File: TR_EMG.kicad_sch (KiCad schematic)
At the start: 7 parts, among them J1 1727230, J2 1727230, J3 1844236, J4 MJ-3523-SMT-TR, J5 MJ-3523-SMT-TR, J6 MJ-3523-SMT-TR, J7 MJ-3523-SMT-TR

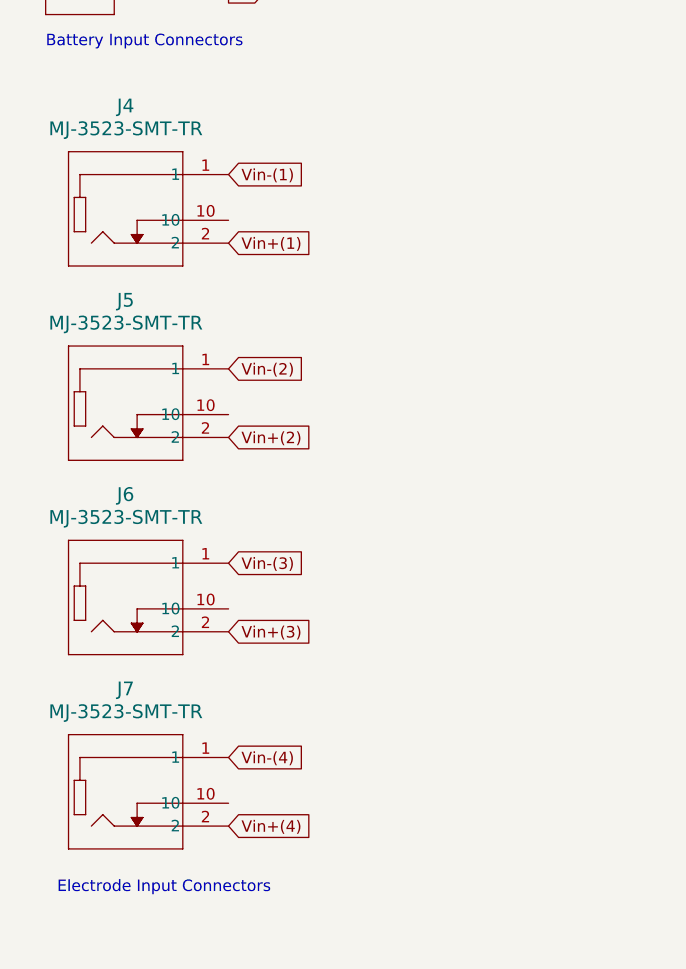
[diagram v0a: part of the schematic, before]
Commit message: first chunk of pcb layout and schematics mods (no connects on pins and changing global labels to hieracarchical labels), one filtering pcb circuit layed out
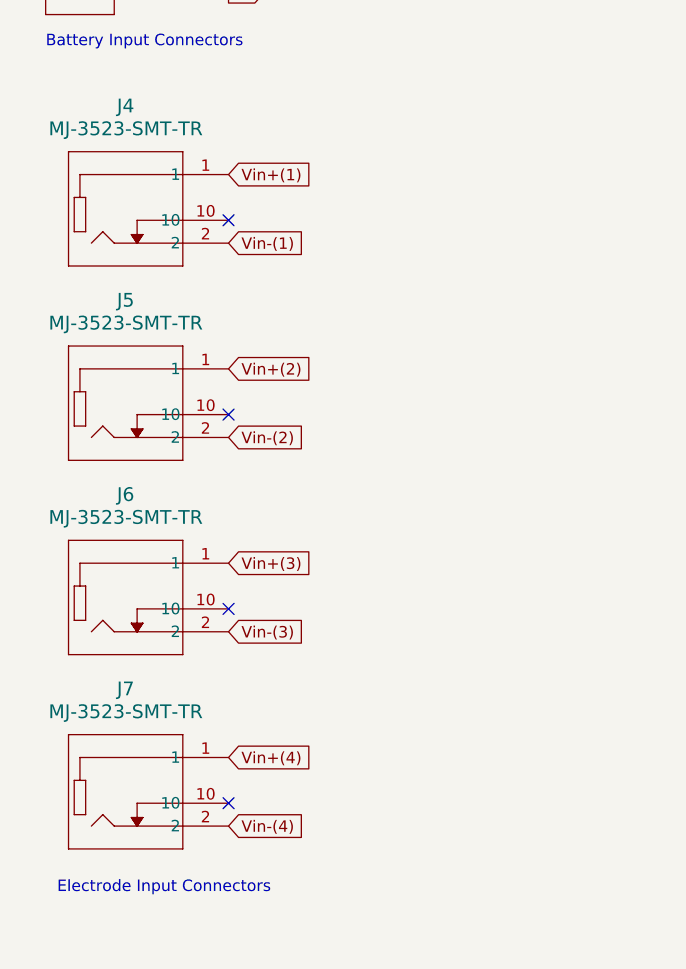
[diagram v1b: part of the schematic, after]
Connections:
- net Vin+(1): now also J4.1; no longer J4.2
- net Vin+(2): now also J5.1; no longer J5.2
- net Vin+(3): now also J6.1; no longer J6.2
- net Vin+(4): now also J7.1; no longer J7.2
- net Vin-(1): now also J4.2; no longer J4.1
- net Vin-(2): now also J5.2; no longer J5.1
- net Vin-(3): now also J6.2; no longer J6.1
- net Vin-(4): now also J7.2; no longer J7.1
- no-connect marks 0 -> 4
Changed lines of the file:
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@@
   (junction (at 30.48 34.29) (diameter 0) (color 0 0 0 0)
   )
+  (no_connect (at 38.1 68.58))
+  (no_connect (at 38.1 133.35))
+  (no_connect (at 38.1 90.17))
+  (no_connect (at 38.1 111.76))
   (wire (pts (xy 262.89 66.04) (xy 269.24 66.04))
     (stroke (width 0) (type default))
@@
     )
   )
+  (global_label "Vin+(3)" (shape input) (at 38.1 106.68 0) (fields_autoplaced)
+    (effects (font (size 1.27 1.27)) (justify left))
+    (property "Intersheetrefs" "${INTERSHEET_REFS}" (at 48.4029 106.68 0)
+      (effects (font (size 1.27 1.27)) (justify left) hide)
+    )
+  )
   (global_label "Vin+(2)" (shape input) (at 157.48 73.66 180) (fields_autoplaced)
     (effects (font (size 1.27 1.27)) (justify right))
@@
     )
   )
-  (global_label "Vin-(1)" (shape input) (at 38.1 63.5 0) (fields_autoplaced)
+  (global_label "Vin-(3)" (shape input) (at 38.1 114.3 0) (fields_autoplaced)
+    (effects (font (size 1.27 1.27)) (justify left))
+    (property "Intersheetrefs" "${INTERSHEET_REFS}" (at 48.4029 114.3 0)
+      (effects (font (size 1.27 1.27)) (justify left) hide)
+    )
+  )
+  (global_label "V-" (shape output) (at 38.1 43.18 0) (fields_autoplaced)
+    (effects (font (size 1.27 1.27)) (justify left))
+    (property "Intersheetrefs" "${INTERSHEET_REFS}" (at 43.7462 43.18 0)
+      (effects (font (size 1.27 1.27)) (justify left) hide)
+    )
+  )
+  (global_label "V-" (shape input) (at 187.96 80.01 270) (fields_autoplaced)
+    (effects (font (size 1.27 1.27)) (justify right))
+    (property "Intersheetrefs" "${INTERSHEET_REFS}" (at 187.96 85.6562 90)
+      (effects (font (size 1.27 1.27)) (justify right) hide)
+    )
+  )
+  (global_label "Vin-(1)" (shape input) (at 38.1 71.12 0) (fields_autoplaced)
+    (effects (font (size 1.27 1.27)) (justify left))
+    (property "Intersheetrefs" "${INTERSHEET_REFS}" (at 48.4029 71.12 0)
+      (effects (font (size 1.27 1.27)) (justify left) hide)
+    )
+  )
+  (global_label "Vin+(1)" (shape input) (at 157.48 41.91 180) (fields_autoplaced)
+    (effects (font (size 1.27 1.27)) (justify right))
+    (property "Intersheetrefs" "${INTERSHEET_REFS}" (at 147.1771 41.91 0)
+      (effects (font (size 1.27 1.27)) (justify right) hide)
+    )
+  )
+  (global_label "Vin+(4)" (shape input) (at 157.48 137.16 180) (fields_autoplaced)
+    (effects (font (size 1.27 1.27)) (justify right))
+    (property "Intersheetrefs" "${INTERSHEET_REFS}" (at 147.1771 137.16 0)
+      (effects (font (size 1.27 1.27)) (justify right) hide)
+    )
+  )
+  (global_label "Vin-(2)" (shape input) (at 157.48 67.31 180) (fields_autoplaced)
+    (effects (font (size 1.27 1.27)) (justify right))
+    (property "Intersheetrefs" "${INTERSHEET_REFS}" (at 147.1771 67.31 0)
+      (effects (font (size 1.27 1.27)) (justify right) hide)
+    )
+  )
+  (global_label "Vin+(2)" (shape input) (at 38.1 85.09 0) (fields_autoplaced)
+    (effects (font (size 1.27 1.27)) (justify left))
+    (property "Intersheetrefs" "${INTERSHEET_REFS}" (at 48.4029 85.09 0)
+      (effects (font (size 1.27 1.27)) (justify left) hide)
+    )
+  )
+  (global_label "V+" (shape output) (at 33.02 24.13 0) (fields_autoplaced)
+    (effects (font (size 1.27 1.27)) (justify left))
+    (property "Intersheetrefs" "${INTERSHEET_REFS}" (at 38.6662 24.13 0)
+      (effects (font (size 1.27 1.27)) (justify left) hide)
+    )
+  )
+  (global_label "V+" (shape input) (at 187.96 29.21 90) (fields_autoplaced)
+    (effects (font (size 1.27 1.27)) (justify left))
+    (property "Intersheetrefs" "${INTERSHEET_REFS}" (at 187.96 23.5638 90)
+      (effects (font (size 1.27 1.27)) (justify left) hide)
+    )
+  )
+  (global_label "Vin+(4)" (shape input) (at 38.1 128.27 0) (fields_autoplaced)
+    (effects (font (size 1.27 1.27)) (justify left))
+    (property "Intersheetrefs" "${INTERSHEET_REFS}" (at 48.4029 128.27 0)
+      (effects (font (size 1.27 1.27)) (justify left) hide)
+    )
+  )
+  (global_label "Vin+(1)" (shape input) (at 38.1 63.5 0) (fields_autoplaced)
     (effects (font (size 1.27 1.27)) (justify left))
     (property "Intersheetrefs" "${INTERSHEET_REFS}" (at 48.4029 63.5 0)
@@
     )
   )
-  (global_label "Vin+(3)" (shape input) (at 38.1 114.3 0) (fields_autoplaced)
-    (effects (font (size 1.27 1.27)) (justify left))
-    (property "Intersheetrefs" "${INTERSHEET_REFS}" (at 48.4029 114.3 0)
-      (effects (font (size 1.27 1.27)) (justify left) hide)
-    )
-  )
-  (global_label "V-" (shape output) (at 38.1 43.18 0) (fields_autoplaced)
-    (effects (font (size 1.27 1.27)) (justify left))
-    (property "Intersheetrefs" "${INTERSHEET_REFS}" (at 43.7462 43.18 0)
-      (effects (font (size 1.27 1.27)) (justify left) hide)
-    )
-  )
-  (global_label "Vin-(2)" (shape input) (at 38.1 85.09 0) (fields_autoplaced)
-    (effects (font (size 1.27 1.27)) (justify left))
-    (property "Intersheetrefs" "${INTERSHEET_REFS}" (at 48.4029 85.09 0)
-      (effects (font (size 1.27 1.27)) (justify left) hide)
-    )
-  )
-  (global_label "V-" (shape input) (at 187.96 80.01 270) (fields_autoplaced)
-    (effects (font (size 1.27 1.27)) (justify right))
-    (property "Intersheetrefs" "${INTERSHEET_REFS}" (at 187.96 85.6562 90)
-      (effects (font (size 1.27 1.27)) (justify right) hide)
-    )
-  )
-  (global_label "Vin-(3)" (shape input) (at 38.1 106.68 0) (fields_autoplaced)
-    (effects (font (size 1.27 1.27)) (justify left))
-    (property "Intersheetrefs" "${INTERSHEET_REFS}" (at 48.4029 106.68 0)
-      (effects (font (size 1.27 1.27)) (justify left) hide)
-    )
-  )
-  (global_label "Vin+(1)" (shape input) (at 157.48 41.91 180) (fields_autoplaced)
-    (effects (font (size 1.27 1.27)) (justify right))
-    (property "Intersheetrefs" "${INTERSHEET_REFS}" (at 147.1771 41.91 0)
-      (effects (font (size 1.27 1.27)) (justify right) hide)
-    )
-  )
-  (global_label "Vin+(4)" (shape input) (at 157.48 137.16 180) (fields_autoplaced)
-    (effects (font (size 1.27 1.27)) (justify right))
-    (property "Intersheetrefs" "${INTERSHEET_REFS}" (at 147.1771 137.16 0)
-      (effects (font (size 1.27 1.27)) (justify right) hide)
-    )
-  )
-  (global_label "Vin-(2)" (shape input) (at 157.48 67.31 180) (fields_autoplaced)
-    (effects (font (size 1.27 1.27)) (justify right))
-    (property "Intersheetrefs" "${INTERSHEET_REFS}" (at 147.1771 67.31 0)
-      (effects (font (size 1.27 1.27)) (justify right) hide)
-    )
-  )
-  (global_label "V+" (shape output) (at 33.02 24.13 0) (fields_autoplaced)
-    (effects (font (size 1.27 1.27)) (justify left))
-    (property "Intersheetrefs" "${INTERSHEET_REFS}" (at 38.6662 24.13 0)
-      (effects (font (size 1.27 1.27)) (justify left) hide)
-    )
-  )
-  (global_label "V+" (shape input) (at 187.96 29.21 90) (fields_autoplaced)
-    (effects (font (size 1.27 1.27)) (justify left))
-    (property "Intersheetrefs" "${INTERSHEET_REFS}" (at 187.96 23.5638 90)
-      (effects (font (size 1.27 1.27)) (justify left) hide)
-    )
-  )
   (global_label "V+" (shape input) (at 187.96 124.46 90) (fields_autoplaced)
     (effects (font (size 1.27 1.27)) (justify left))
@@
     )
   )
-  (global_label "Vin+(4)" (shape input) (at 38.1 135.89 0) (fields_autoplaced)
+  (global_label "V-" (shape input) (at 187.96 143.51 270) (fields_autoplaced)
+    (effects (font (size 1.27 1.27)) (justify right))
+    (property "Intersheetrefs" "${INTERSHEET_REFS}" (at 187.96 149.1562 90)
+      (effects (font (size 1.27 1.27)) (justify right) hide)
+    )
+  )
+  (global_label "Vin-(4)" (shape input) (at 38.1 135.89 0) (fields_autoplaced)
     (effects (font (size 1.27 1.27)) (justify left))
     (property "Intersheetrefs" "${INTERSHEET_REFS}" (at 48.4029 135.89 0)
@@
     )
   )
-  (global_label "V-" (shape input) (at 187.96 143.51 270) (fields_autoplaced)
-    (effects (font (size 1.27 1.27)) (justify right))
-    (property "Intersheetrefs" "${INTERSHEET_REFS}" (at 187.96 149.1562 90)
-      (effects (font (size 1.27 1.27)) (justify right) hide)
-    )
-  )
-  (global_label "Vin-(4)" (shape input) (at 38.1 128.27 0) (fields_autoplaced)
-    (effects (font (size 1.27 1.27)) (justify left))
-    (property "Intersheetrefs" "${INTERSHEET_REFS}" (at 48.4029 128.27 0)
-      (effects (font (size 1.27 1.27)) (justify left) hide)
-    )
-  )
-  (global_label "Vin+(1)" (shape input) (at 38.1 71.12 0) (fields_autoplaced)
-    (effects (font (size 1.27 1.27)) (justify left))
-    (property "Intersheetrefs" "${INTERSHEET_REFS}" (at 48.4029 71.12 0)
+  (global_label "Vin-(2)" (shape input) (at 38.1 92.71 0) (fields_autoplaced)
+    (effects (font (size 1.27 1.27)) (justify left))
+    (property "Intersheetrefs" "${INTERSHEET_REFS}" (at 48.4029 92.71 0)
       (effects (font (size 1.27 1.27)) (justify left) hide)
     )
@@
       (effects (font (size 1.27 1.27)) (justify left) hide)
     )
-  )
-  (global_label "Vin+(2)" (shape input) (at 38.1 92.71 0) (fields_autoplaced)
-    (effects (font (size 1.27 1.27)) (justify left))
-    (property "Intersheetrefs" "${INTERSHEET_REFS}" (at 48.4029 92.71 0)
-      (effects (font (size 1.27 1.27)) (justify left) hide)
-    )

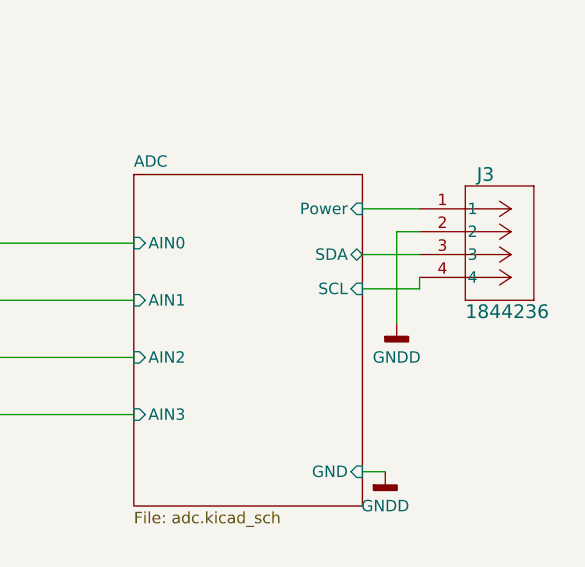
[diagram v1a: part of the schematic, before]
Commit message: finished majority of layout, pcb expanded to four copper layers to accomadate power planes
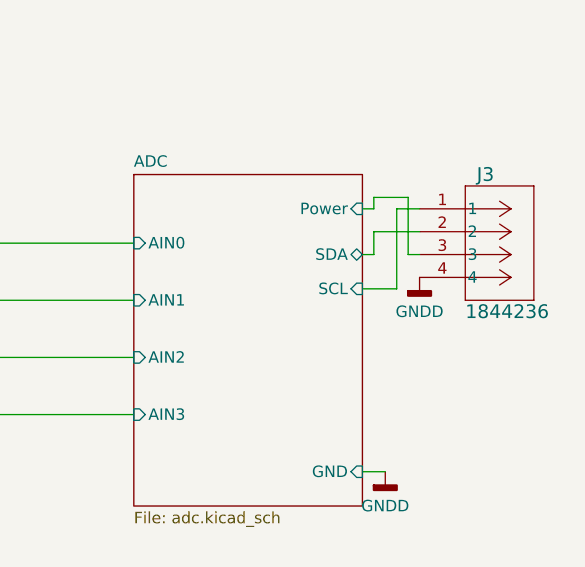
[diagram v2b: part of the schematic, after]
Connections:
- net ADC/Power: now also J3.3; no longer J3.1
- net ADC/SCL: now also J3.1; no longer J3.4
- net ADC/SDA: now also J3.2; no longer J3.3
- net GNDD: now also J3.4; no longer J3.2
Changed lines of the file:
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@@
   (no_connect (at 38.1 90.17))
   (no_connect (at 38.1 111.76))
-  (wire (pts (xy 262.89 66.04) (xy 269.24 66.04))
+  (wire (pts (xy 267.97 66.04) (xy 269.24 66.04))
     (stroke (width 0) (type default))
   )
@@
     (stroke (width 0) (type default))
   )
-  (wire (pts (xy 262.89 69.85) (xy 269.24 69.85))
+  (wire (pts (xy 262.89 60.96) (xy 264.16 60.96))
     (stroke (width 0) (type default))
   )
@@
     (stroke (width 0) (type default))
   )
+  (wire (pts (xy 264.16 59.69) (xy 267.97 59.69))
+    (stroke (width 0) (type default))
+  )
+  (wire (pts (xy 266.7 69.85) (xy 266.7 60.96))
+    (stroke (width 0) (type default))
+  )
   (wire (pts (xy 30.48 34.29) (xy 30.48 40.64))
     (stroke (width 0) (type default))
   )
+  (wire (pts (xy 264.16 66.04) (xy 264.16 63.5))
+    (stroke (width 0) (type default))
+  )
   (wire (pts (xy 187.96 124.46) (xy 187.96 125.73))
     (stroke (width 0) (type default))
@@
     (stroke (width 0) (type default))
   )
-  (wire (pts (xy 269.24 63.5) (xy 266.7 63.5))
-    (stroke (width 0) (type default))
-  )
   (wire (pts (xy 193.04 134.62) (xy 220.98 134.62))
     (stroke (width 0) (type default))
@@
     (stroke (width 0) (type default))
   )
-  (wire (pts (xy 269.24 68.58) (xy 269.24 69.85))
-    (stroke (width 0) (type default))
-  )
   (wire (pts (xy 237.49 64.77) (xy 207.01 64.77))
     (stroke (width 0) (type default))
   )
+  (wire (pts (xy 264.16 60.96) (xy 264.16 59.69))
+    (stroke (width 0) (type default))
+  )
+  (wire (pts (xy 267.97 59.69) (xy 267.97 66.04))
+    (stroke (width 0) (type default))
+  )
   (wire (pts (xy 207.01 102.87) (xy 207.01 77.47))
     (stroke (width 0) (type default))
@@
     (stroke (width 0) (type default))
   )
+  (wire (pts (xy 262.89 66.04) (xy 264.16 66.04))
+    (stroke (width 0) (type default))
+  )
   (wire (pts (xy 187.96 110.49) (xy 187.96 111.76))
     (stroke (width 0) (type default))
   )
-  (wire (pts (xy 266.7 63.5) (xy 266.7 73.66))
-    (stroke (width 0) (type default))
-  )
-  (wire (pts (xy 262.89 60.96) (xy 269.24 60.96))
+  (wire (pts (xy 262.89 69.85) (xy 266.7 69.85))
+    (stroke (width 0) (type default))
+  )
+  (wire (pts (xy 266.7 60.96) (xy 269.24 60.96))
     (stroke (width 0) (type default))
   )
@@
   )
   (wire (pts (xy 193.04 102.87) (xy 207.01 102.87))
+    (stroke (width 0) (type default))
+  )
+  (wire (pts (xy 264.16 63.5) (xy 269.24 63.5))
     (stroke (width 0) (type default))
   )
@@
     )
   )
-  (symbol (lib_id "power:GNDD") (at 266.7 73.66 0) (unit 1)
-    (in_bom yes) (on_board yes) (dnp no) (fields_autoplaced)
-    (property "Reference" "#PWR015" (at 266.7 80.01 0)
-      (effects (font (size 1.27 1.27)) hide)
-    )
-    (property "Value" "GNDD" (at 266.7 77.47 0)
+  (symbol (lib_id "power:GNDD") (at 269.24 68.58 0) (unit 1)
+    (in_bom yes) (on_board yes) (dnp no) (fields_autoplaced)
+    (property "Reference" "#PWR015" (at 269.24 74.93 0)
+      (effects (font (size 1.27 1.27)) hide)
+    )
+    (property "Value" "GNDD" (at 269.24 72.39 0)
       (effects (font (size 1.27 1.27)))
     )
-    (property "Footprint" "" (at 266.7 73.66 0)
-      (effects (font (size 1.27 1.27)) hide)
-    )
-    (property "Datasheet" "" (at 266.7 73.66 0)
-      (effects (font (size 1.27 1.27)) hide)
-    )
+    (property "Footprint" "" (at 269.24 68.58 0)
+      (effects (font (size 1.27 1.27)) hide)
+    )
+    (property "Datasheet" "" (at 269.24 68.58 0)
+      (effects (font (size 1.27 1.27)) hide)
+    )

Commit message: ToTheEdge,LCSCNums
Moved the 3.5mm connectors to the edge and edited their footprint courtyard so no errors. Adjusted the planes so that it bordered 3.5mm connector pads well and didn't go to edge cuts. Added LCSC part numbers to the parts that were in stock.
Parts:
- J4, J5, J6, J7: footprint footprints:CONN_MJ-3523_CUD -> footprints:CONN_MJ-3523_CUD_CtYrd
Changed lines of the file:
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@@
       (effects (font (size 1.524 1.524)))
     )
-    (property "Footprint" "footprints:CONN_MJ-3523_CUD" (at 38.1 85.09 0)
+    (property "Footprint" "footprints:CONN_MJ-3523_CUD_CtYrd" (at 38.1 85.09 0)
       (effects (font (size 1.27 1.27) italic) hide)
     )
@@
       (effects (font (size 1.27 1.27) italic) hide)
     )
+    (property "LCSC" "" (at 38.1 85.09 0)
+      (effects (font (size 1.27 1.27)) hide)
+    )
     (pin "2")
     (pin "1")
@@
       (effects (font (size 1.27 1.27) italic) hide)
     )
+    (property "LCSC" "" (at 30.48 40.64 0)
+      (effects (font (size 1.27 1.27)) hide)
+    )
     (pin "2")
     (pin "1")
@@
       (effects (font (size 1.524 1.524)))
     )
-    (property "Footprint" "footprints:CONN_MJ-3523_CUD" (at 38.1 106.68 0)
+    (property "Footprint" "footprints:CONN_MJ-3523_CUD_CtYrd" (at 38.1 106.68 0)
       (effects (font (size 1.27 1.27) italic) hide)
     )
     (property "Datasheet" "MJ-3523-SMT-TR" (at 38.1 106.68 0)
       (effects (font (size 1.27 1.27) italic) hide)
+    )
+    (property "LCSC" "" (at 38.1 106.68 0)
+      (effects (font (size 1.27 1.27)) hide)
     )
     (pin "2")
@@
       (effects (font (size 1.524 1.524)))
     )
-    (property "Footprint" "footprints:CONN_MJ-3523_CUD" (at 38.1 63.5 0)
+    (property "Footprint" "footprints:CONN_MJ-3523_CUD_CtYrd" (at 38.1 63.5 0)
       (effects (font (size 1.27 1.27) italic) hide)
     )
     (property "Datasheet" "MJ-3523-SMT-TR" (at 38.1 63.5 0)
       (effects (font (size 1.27 1.27) italic) hide)
+    )
+    (property "LCSC" "" (at 38.1 63.5 0)
+      (effects (font (size 1.27 1.27)) hide)
     )
     (pin "2")
@@
     (property "Datasheet" "1727230" (at 30.48 24.13 0)
       (effects (font (size 1.27 1.27) italic) hide)
+    )
+    (property "LCSC" "" (at 30.48 24.13 0)
+      (effects (font (size 1.27 1.27)) hide)
     )
     (pin "2")
@@
       (effects (font (size 1.27 1.27) italic) hide)
     )
+    (property "LCSC" "" (at 269.24 60.96 0)
+      (effects (font (size 1.27 1.27)) hide)
+    )
     (pin "3")
     (pin "4")
@@
       (effects (font (size 1.524 1.524)))
     )
-    (property "Footprint" "footprints:CONN_MJ-3523_CUD" (at 38.1 128.27 0)
+    (property "Footprint" "footprints:CONN_MJ-3523_CUD_CtYrd" (at 38.1 128.27 0)
       (effects (font (size 1.27 1.27) italic) hide)
     )
@@
       (effects (font (size 1.27 1.27) italic) hide)
     )
-    (pin "2")
+    (property "LCSC" "" (at 38.1 128.27 0)
+      (effects (font (size 1.27 1.27)) hide)
+    )
+    (pin "2")
